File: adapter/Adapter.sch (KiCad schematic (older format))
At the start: 50 parts, among them J1 USB_B_Micro, J2 2040210-1, J3 USB_C_Receptacle, J4 Conn_01x05_Male, Q1 IRLML2244TRPBF, SW1 SW_Push, SW2 SW_Push, U1 SN75DP119, U2 AZ1117-3.3, U3 STM32F072C8Tx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

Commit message: more 3d packages...
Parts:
- added C17: 100n, Capacitor_SMD:C_0603_1608Metric_Pad1.05x0.95mm_HandSolder, symbol Device:C_Small
- added J5: Conn_01x03_Male, Connector_Molex:Molex_PicoBlade_53047-0310_1x03_P1.25mm_Vertical, symbol Connector:Conn_01x03_Male
- J4: footprint Connector_PinHeader_2.54mm:PinHeader_1x05_P2.54mm_Vertical -> Connector_Molex:Molex_PicoBlade_53047-0510_1x05_P1.25mm_Vertical
- SW1, SW2: footprint Button_Switch_SMD:SW_SPST_PTS645 -> EVQPLMA15:EVQPLMA15; MFP PTS647SN38SMTR2LFS -> EVQ-PLMA15
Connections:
- net GND: now also C17.2, J5.1 (Pin_1)
- net UART_RX: now also J5.2 (Pin_2)
- net UART_TX: now also J5.3 (Pin_3)
- net at C1.1, L1.1, U1.11 (VCC)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: now also C17.1
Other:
- moved on the sheet: C4, J4, L1
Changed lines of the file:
@@
 L Device:Ferrite_Bead_Small L1
 U 1 1 5C516BF3
-P 6100 2450
-F 0 "L1" V 5863 2450 50  0000 C CNN
-F 1 "CIM05U601NC" V 6150 2350 50  0000 C CNN
-F 2 "Inductor_SMD:L_0603_1608Metric_Pad1.05x0.95mm_HandSolder" V 6030 2450 50  0001 C CNN
-F 3 "~" H 6100 2450 50  0001 C CNN
-	1    6100 2450
+P 6150 2300
+F 0 "L1" V 5913 2300 50  0000 C CNN
+F 1 "CIM05U601NC" V 6200 2200 50  0000 C CNN
+F 2 "Inductor_SMD:L_0603_1608Metric_Pad1.05x0.95mm_HandSolder" V 6080 2300 50  0001 C CNN
+F 3 "~" H 6150 2300 50  0001 C CNN
+	1    6150 2300
 	0    1    1    0
 $EndComp
@@
 Connection ~ 6550 2450
 Connection ~ 6300 2450
-Wire Wire Line
-	6300 2450 6200 2450
 $Comp
 L power:+3V3 #PWR0110
 U 1 1 5C51B455
-P 5900 2350
-F 0 "#PWR0110" H 5900 2200 50  0001 C CNN
-F 1 "+3V3" H 5915 2523 50  0000 C CNN
-F 2 "" H 5900 2350 50  0001 C CNN
-F 3 "" H 5900 2350 50  0001 C CNN
-	1    5900 2350
-	1    0    0    -1
-$EndComp
-Wire Wire Line
-	5900 2350 5900 2450
-Wire Wire Line
-	5900 2450 6000 2450
+P 6000 2250
+F 0 "#PWR0110" H 6000 2100 50  0001 C CNN
+F 1 "+3V3" H 6015 2423 50  0000 C CNN
+F 2 "" H 6000 2250 50  0001 C CNN
+F 3 "" H 6000 2250 50  0001 C CNN
+	1    6000 2250
+	1    0    0    -1
+$EndComp
 Text Label 8100 1850 0    50   ~ 0
 DP_OUT_0+
@@
 Wire Wire Line
 	10000 1000 10000 1150
-Text Label 7000 5750 2    50   ~ 0
+Text Label 7050 4950 2    50   ~ 0
 EXT_3.3V
-Text Label 7000 5850 2    50   ~ 0
+Text Label 7050 5050 2    50   ~ 0
 SWCLK
 $Comp
 L power:GND #PWR0105
 U 1 1 5C53D6AA
-P 6650 6400
-F 0 "#PWR0105" H 6650 6150 50  0001 C CNN
-F 1 "GND" H 6655 6227 50  0000 C CNN
-F 2 "" H 6650 6400 50  0001 C CNN
-F 3 "" H 6650 6400 50  0001 C CNN
-	1    6650 6400
-	1    0    0    -1
-$EndComp
-Text Label 7000 6050 2    50   ~ 0
+P 6700 5600
+F 0 "#PWR0105" H 6700 5350 50  0001 C CNN
+F 1 "GND" H 6705 5427 50  0000 C CNN
+F 2 "" H 6700 5600 50  0001 C CNN
+F 3 "" H 6700 5600 50  0001 C CNN
+	1    6700 5600
+	1    0    0    -1
+$EndComp
+Text Label 7050 5250 2    50   ~ 0
 SWDIO
-Text Label 7000 6150 2    50   ~ 0
+Text Label 7050 5350 2    50   ~ 0
 nRESET
 $Comp
 L Connector:Conn_01x05_Male J4
 U 1 1 5C53F02C
-P 7200 5950
-F 0 "J4" H 7173 5973 50  0000 R CNN
-F 1 "Conn_01x05_Male" H 7173 5882 50  0000 R CNN
-F 2 "Connector_PinHeader_2.54mm:PinHeader_1x05_P2.54mm_Vertical" H 7200 5950 50  0001 C CNN
-F 3 "~" H 7200 5950 50  0001 C CNN
-	1    7200 5950
+P 7250 5150
+F 0 "J4" H 7223 5173 50  0000 R CNN
+F 1 "Conn_01x05_Male" H 7223 5082 50  0000 R CNN
+F 2 "Connector_Molex:Molex_PicoBlade_53047-0510_1x05_P1.25mm_Vertical" H 7250 5150 50  0001 C CNN
+F 3 "~" H 7250 5150 50  0001 C CNN
+	1    7250 5150
 	-1   0    0    -1
 $EndComp
-Text Notes 7200 6350 0    50   ~ 0
+Text Notes 7250 5550 0    50   ~ 0
 SWD Connector\nCheck congruence with nucleo board??\nSTMboards have 6 pins??
 $Comp
@@
 L Device:C_Small C4
 U 1 1 5C5A8D80
-P 6800 6250
-F 0 "C4" H 6650 6300 50  0000 L CNN
-F 1 "100n" H 6600 6200 50  0000 L CNN
-F 2 "Capacitor_SMD:C_0603_1608Metric_Pad1.05x0.95mm_HandSolder" H 6800 6250 50  0001 C CNN
-F 3 "~" H 6800 6250 50  0001 C CNN
-	1    6800 6250
-	1    0    0    -1
-$EndComp
-Wire Wire Line
-	6650 6350 6800 6350
-Connection ~ 6650 6350
-Wire Wire Line
-	7000 6150 6800 6150
-Wire Wire Line
-	6650 6400 6650 6350
-Wire Wire Line
-	6650 5950 7000 5950
-Wire Wire Line
-	6650 5950 6650 6350
+P 6850 5450
+F 0 "C4" H 6700 5500 50  0000 L CNN
+F 1 "100n" H 6650 5400 50  0000 L CNN
+F 2 "Capacitor_SMD:C_0603_1608Metric_Pad1.05x0.95mm_HandSolder" H 6850 5450 50  0001 C CNN
+F 3 "~" H 6850 5450 50  0001 C CNN
+	1    6850 5450
+	1    0    0    -1
+$EndComp
+Wire Wire Line
+	6700 5550 6850 5550
+Connection ~ 6700 5550
+Wire Wire Line
+	7050 5350 6850 5350
+Wire Wire Line
+	6700 5600 6700 5550
+Wire Wire Line
+	6700 5150 7050 5150
+Wire Wire Line
+	6700 5150 6700 5550
 $Comp
 L Device:R R2
@@
 F 0 "SW1" V 5554 6448 50  0000 L CNN
 F 1 "SW_Push" V 5645 6448 50  0000 L CNN
-F 2 "Button_Switch_SMD:SW_SPST_PTS645" H 5600 6500 50  0001 C CNN
+F 2 "EVQPLMA15:EVQPLMA15" H 5600 6500 50  0001 C CNN
 F 3 "" H 5600 6500 50  0001 C CNN
-F 4 "PTS647SN38SMTR2LFS" H 5600 6300 50  0001 C CNN "MFP"
+F 4 "EVQ-PLMA15" H 5600 6300 50  0001 C CNN "MFP"
 	1    5600 6300
 	0    1    1    0
@@
 F 0 "SW2" V 4904 5948 50  0000 L CNN
 F 1 "SW_Push" V 4995 5948 50  0000 L CNN
-F 2 "Button_Switch_SMD:SW_SPST_PTS645" H 4950 6000 50  0001 C CNN
+F 2 "EVQPLMA15:EVQPLMA15" H 4950 6000 50  0001 C CNN
 F 3 "" H 4950 6000 50  0001 C CNN
-F 4 "PTS647SN38SMTR2LFS" H 4950 5800 50  0001 C CNN "MFP"
+F 4 "EVQ-PLMA15" H 4950 5800 50  0001 C CNN "MFP"
 	1    4950 5800
 	0    1    1    0
@@
 Wire Wire Line
 	2550 2150 3000 2150
+$Comp
+L Connector:Conn_01x03_Male J5
+U 1 1 5C591D0F
+P 7050 6200
+F 0 "J5" H 7023 6130 50  0000 R CNN
+F 1 "Conn_01x03_Male" H 7023 6221 50  0000 R CNN
+F 2 "Connector_Molex:Molex_PicoBlade_53047-0310_1x03_P1.25mm_Vertical" H 7050 6200 50  0001 C CNN
+F 3 "~" H 7050 6200 50  0001 C CNN
+	1    7050 6200
+	-1   0    0    1
+$EndComp
+$Comp
+L power:GND #PWR0128
+U 1 1 5C5ABE7E
+P 6700 6450
+F 0 "#PWR0128" H 6700 6200 50  0001 C CNN
+F 1 "GND" H 6705 6277 50  0000 C CNN
+F 2 "" H 6700 6450 50  0001 C CNN
+F 3 "" H 6700 6450 50  0001 C CNN
+	1    6700 6450
+	1    0    0    -1
+$EndComp
+Wire Wire Line
+	6700 6450 6700 6300
+Wire Wire Line
+	6700 6300 6850 6300
+Text Label 6700 6100 2    50   ~ 0
+UART_TX
+Text Label 6700 6200 2    50   ~ 0
+UART_RX
+Wire Wire Line
+	6700 6200 6850 6200
+Wire Wire Line
+	6850 6100 6700 6100
+$Comp
+L Device:C_Small C17
+U 1 1 5C5EF1A2
+P 6150 2550
+F 0 "C17" H 6000 2600 50  0000 L CNN
+F 1 "100n" H 5950 2500 50  0000 L CNN
+F 2 "Capacitor_SMD:C_0603_1608Metric_Pad1.05x0.95mm_HandSolder" H 6150 2550 50  0001 C CNN
+F 3 "~" H 6150 2550 50  0001 C CNN
+	1    6150 2550
+	1    0    0    -1
+$EndComp
+Wire Wire Line
+	6150 2650 6150 2700
+Wire Wire Line
+	6150 2700 6300 2700
+Connection ~ 6300 2700
+Wire Wire Line
+	6150 2450 6300 2450
+Wire Wire Line
+	6000 2250 6000 2300
+Wire Wire Line
+	6000 2300 6050 2300
+Wire Wire Line
+	6250 2300 6300 2300
+Wire Wire Line
+	6300 2300 6300 2450
 $EndSCHEMATC

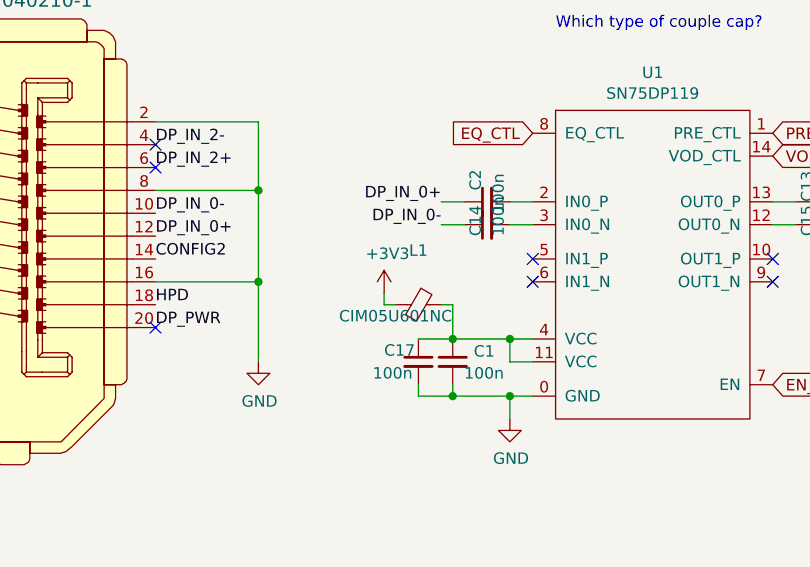
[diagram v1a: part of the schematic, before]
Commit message: remove the bead for the DP119
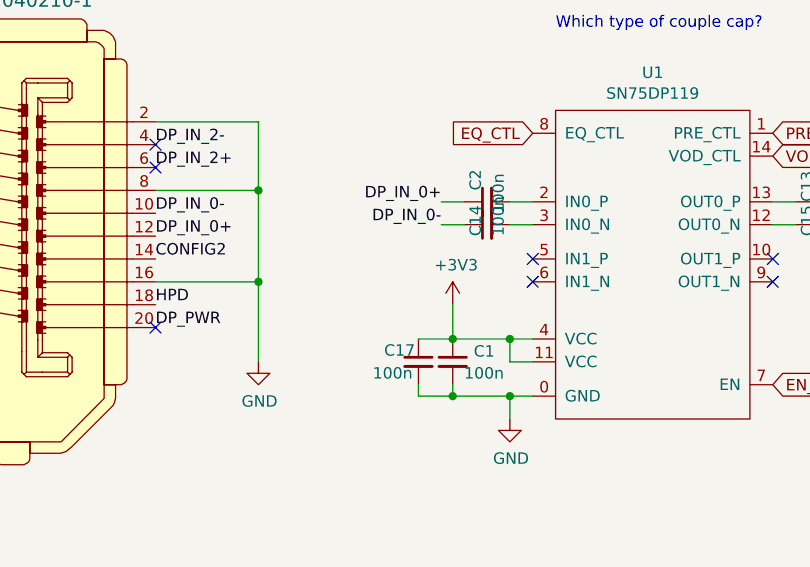
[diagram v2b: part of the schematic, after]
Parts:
- removed L1: CIM05U601NC, Inductor_SMD:L_0603_1608Metric_Pad1.05x0.95mm_HandSolder, symbol Device:Ferrite_Bead_Small
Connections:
- net +3V3: now also C1.1, C17.1, U1.11 (VCC), U1.4 (VCC)
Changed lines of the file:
@@
 	6550 2700 6650 2700
-$Comp
-L Device:Ferrite_Bead_Small L1
-U 1 1 5C516BF3
-P 6150 2300
-F 0 "L1" V 5913 2300 50  0000 C CNN
-F 1 "CIM05U601NC" V 6200 2200 50  0000 C CNN
-F 2 "Inductor_SMD:L_0603_1608Metric_Pad1.05x0.95mm_HandSolder" V 6080 2300 50  0001 C CNN
-F 3 "~" H 6150 2300 50  0001 C CNN
-	1    6150 2300
-	0    1    1    0
-$EndComp
 $Comp
 L Device:C_Small C2
@@
 L power:+3V3 #PWR0110
 U 1 1 5C51B455
-P 6000 2250
-F 0 "#PWR0110" H 6000 2100 50  0001 C CNN
-F 1 "+3V3" H 6015 2423 50  0000 C CNN
-F 2 "" H 6000 2250 50  0001 C CNN
-F 3 "" H 6000 2250 50  0001 C CNN
-	1    6000 2250
+P 6300 2300
+F 0 "#PWR0110" H 6300 2150 50  0001 C CNN
+F 1 "+3V3" H 6315 2473 50  0000 C CNN
+F 2 "" H 6300 2300 50  0001 C CNN
+F 3 "" H 6300 2300 50  0001 C CNN
+	1    6300 2300
 	1    0    0    -1
 $EndComp
@@
 	6150 2450 6300 2450
 Wire Wire Line
-	6000 2250 6000 2300
-Wire Wire Line
-	6000 2300 6050 2300
-Wire Wire Line
-	6250 2300 6300 2300
-Wire Wire Line
 	6300 2300 6300 2450

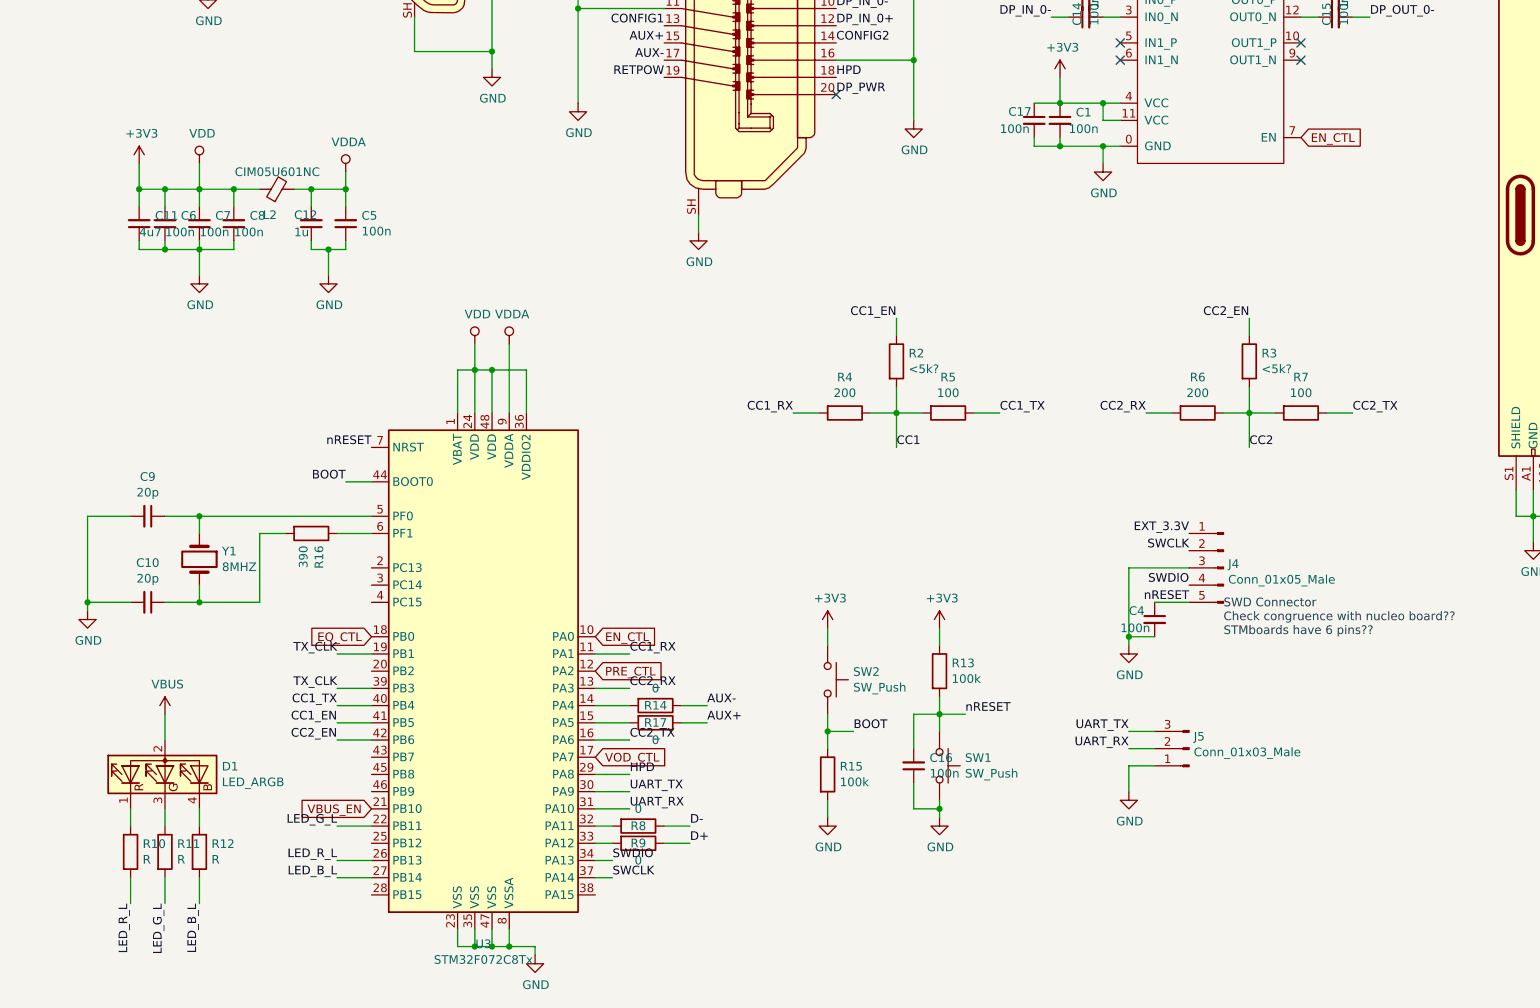
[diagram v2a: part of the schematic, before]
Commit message: Added 2 missing STEP files
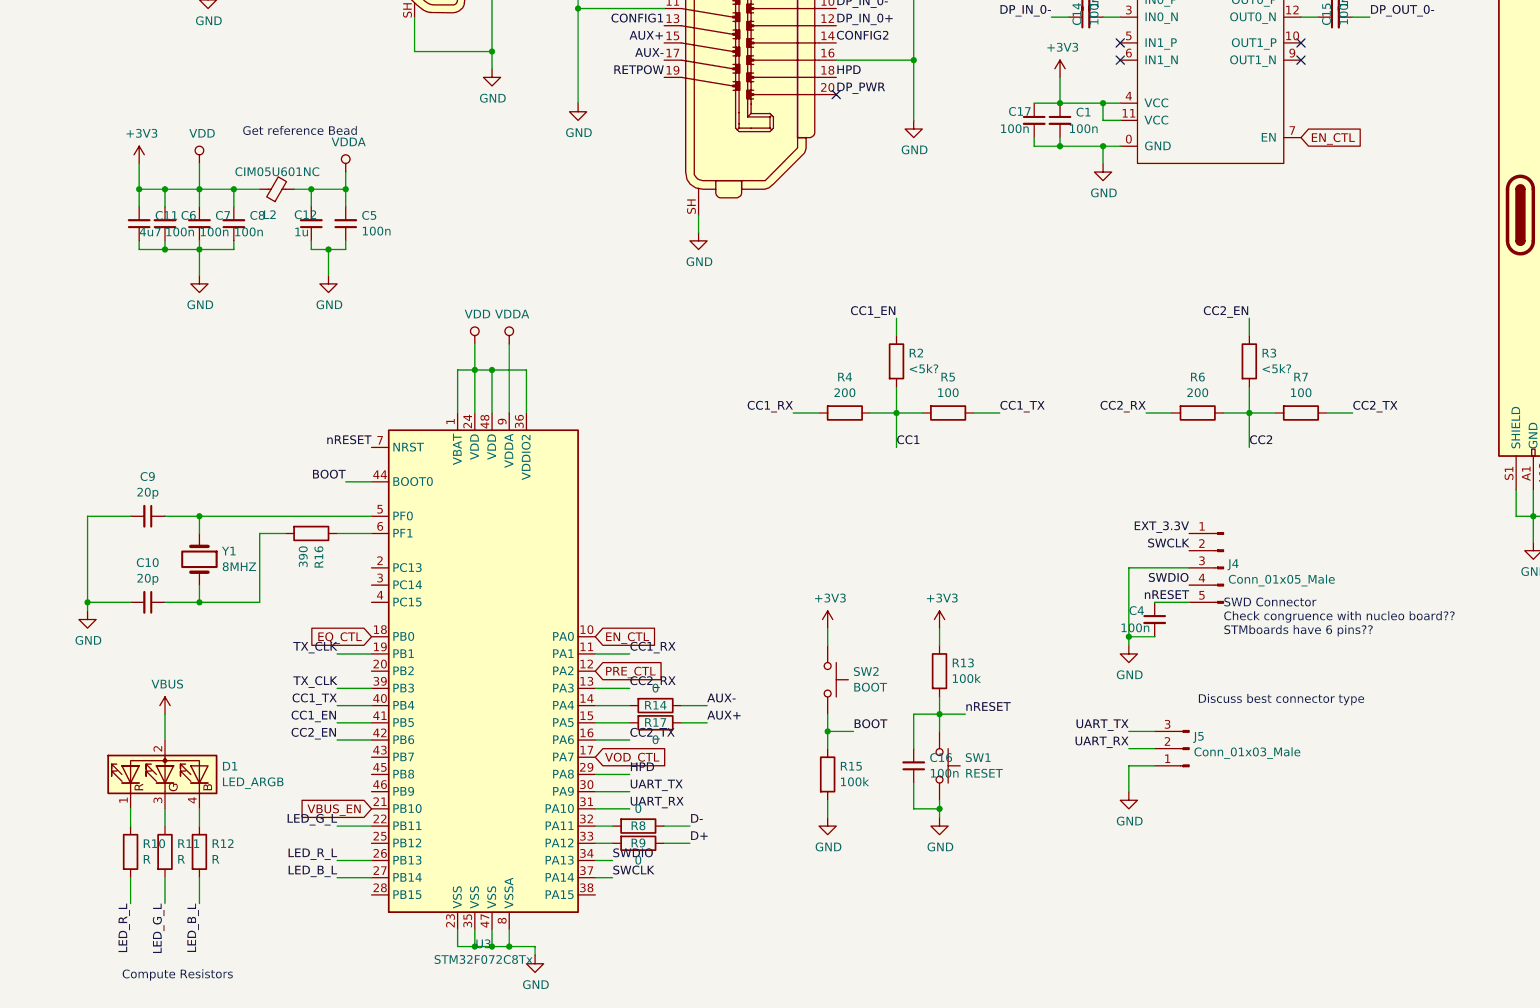
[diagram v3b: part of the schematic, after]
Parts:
- SW1: value SW_Push -> RESET
- SW2: value SW_Push -> BOOT
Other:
- note added: "Compute Resistors\n"
- note added: "Discuss best connector type"
- note added: "Get reference Bead"
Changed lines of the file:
@@
 P 5600 6300
 F 0 "SW1" V 5554 6448 50  0000 L CNN
-F 1 "SW_Push" V 5645 6448 50  0000 L CNN
+F 1 "RESET" V 5645 6448 50  0000 L CNN
 F 2 "EVQPLMA15:EVQPLMA15" H 5600 6500 50  0001 C CNN
 F 3 "" H 5600 6500 50  0001 C CNN
@@
 P 4950 5800
 F 0 "SW2" V 4904 5948 50  0000 L CNN
-F 1 "SW_Push" V 4995 5948 50  0000 L CNN
+F 1 "BOOT" V 4995 5948 50  0000 L CNN
 F 2 "EVQPLMA15:EVQPLMA15" H 4950 6000 50  0001 C CNN
 F 3 "" H 4950 6000 50  0001 C CNN
@@
 Wire Wire Line
 	6300 2300 6300 2450
+Text Notes 1550 2650 0    50   ~ 0
+Get reference Bead
+Text Notes 7100 5950 0    50   ~ 0
+Discuss best connector type
+Text Notes 850  7550 0    50   ~ 0
+Compute Resistors\n
 $EndSCHEMATC
